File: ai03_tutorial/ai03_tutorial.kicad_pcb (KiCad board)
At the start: 2 copper layers, 24 parts, among them SW1 SW_Push, U1 ATmega32U4-AU, Y1 16Mhz

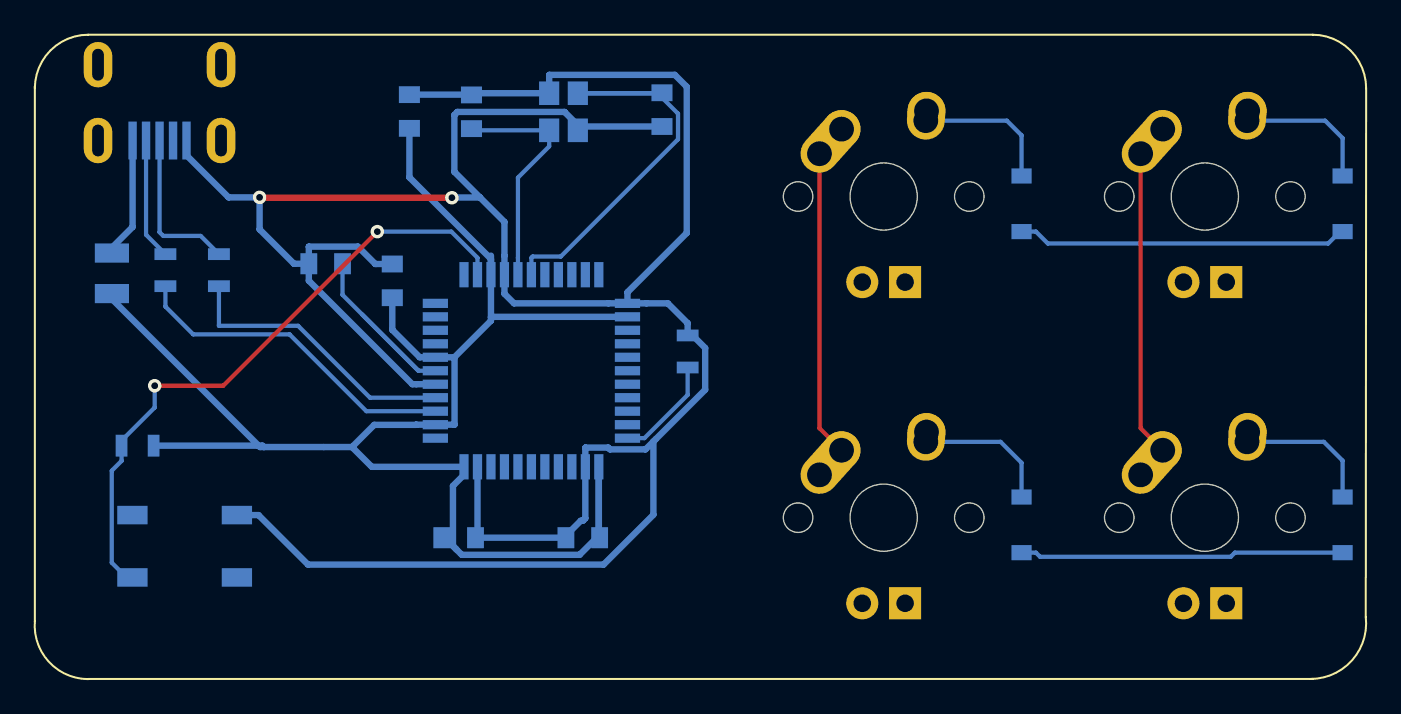
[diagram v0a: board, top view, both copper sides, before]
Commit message: Add new usb connector and plug keycaps
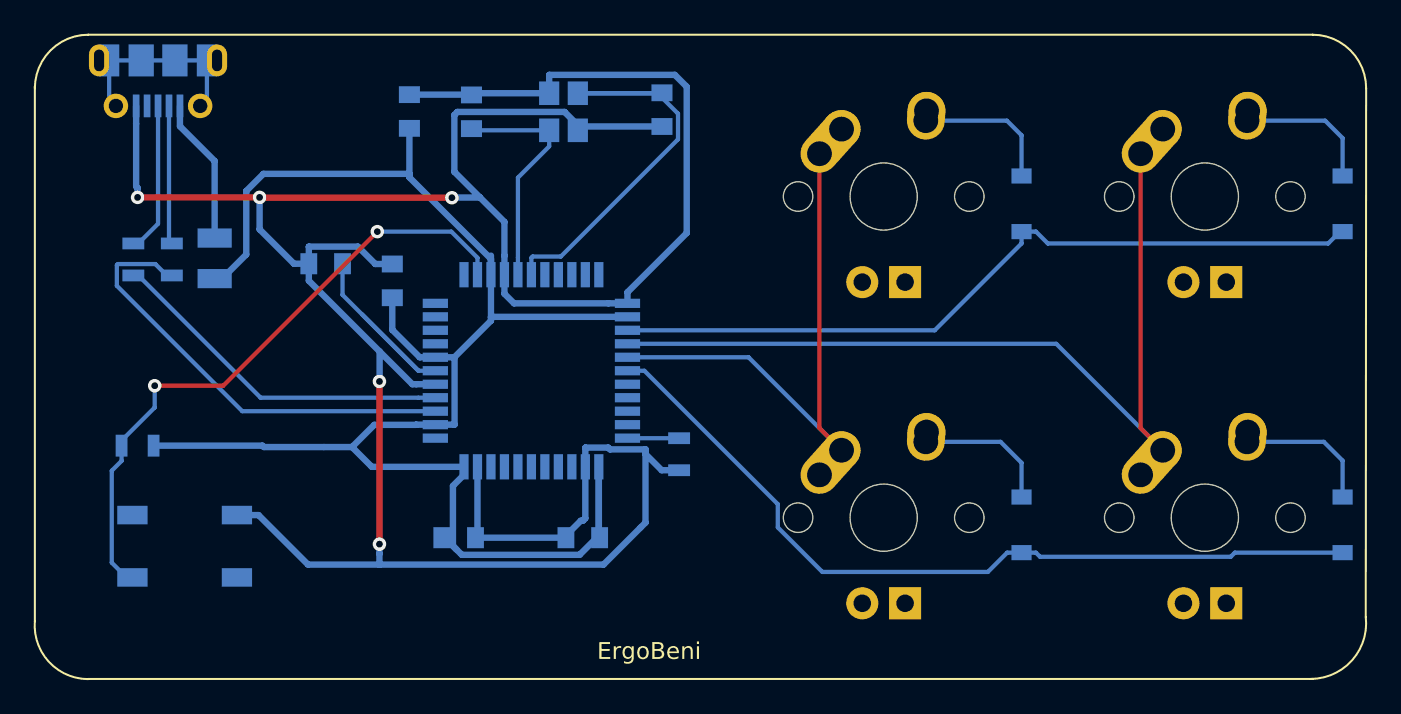
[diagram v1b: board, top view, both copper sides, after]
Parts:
- USB1: footprint random-keyboard-parts:Molex-0548190589 -> Connector_USB:USB_Micro-B_Molex-105017-0001
- moved F1 6.16 mm to (99.6, 89.2)
- moved R4 6.12 mm to (127.1, 100.8), turned to 90 degrees
- moved R2 5.12 mm to (94.7, 89.3)
- moved USB1 0.99 mm to (96.2, 78.7), turned to 0 degrees
- moved R1 0.74 mm to (97.0, 89.3)
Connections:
- U1 pad 25: (no net) -> ROW0
- U1 pad 26: (no net) -> COL1
- U1 pad 27: (no net) -> COL0
- U1 pad 28: (no net) -> ROW1
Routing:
- net COL1: track 18.1 -> 52.5 mm
- net ROW1: track 19.3 -> 48.9 mm
- net ROW0: track 19.6 -> 45.9 mm
- net COL0: track 18.1 -> 33.1 mm
- net Net-(USB1-Pad6): track 0.00 -> 12.1 mm
- net GND: track 171.4 -> 178.9 mm, vias 2 -> 5
- net Net-(R1-Pad1): track 19.8 -> 26.8 mm
- net Net-(R2-Pad1): track 17.0 -> 20.9 mm
- net Net-(R4-Pad2): track 6.26 -> 3.06 mm
- net +5V: track 98.9 -> 101.7 mm
- net D-: track 7.22 -> 8.23 mm
- net VCC: track 7.76 -> 8.69 mm
- net D+: track 9.50 -> 8.94 mm
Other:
- board text added: "ErgoBeni"

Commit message: Add first version : waiting for review
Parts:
- added G***: LOGO, logo:shiba_from_bmp_3, F.Cu at (106.0, 110.0)
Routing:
- added copper zone on B.Cu, net GND
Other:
- board text added: "PCB Keyboard test Benoit V1"
- board text removed: "ErgoBeni"
